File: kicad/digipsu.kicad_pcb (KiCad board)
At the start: 2 copper layers, 137.2 x 174.1 mm, 114 parts, among them J1 Screw_Terminal_01x03, J2 PWR IN, J3 8P8C, J4 8P8C, J5 8P8C, Q1 BC327, Q2 BC337, Q3 2N6058, Q4 2N6058, Q5 IRLZ34N, SW1 RotaryEncoder_Switch, SW2 RotaryEncoder_Switch, U1 INA169, U10 Pico, U11 M24C32-RMN, U12 SN75176BP, U13 6N137, U14 SN75176BP, U15 SN75176BP, U2 MCP6002-xP, U3 Pico, U4 MCP6002-xP, U5 L7805, U6 MCP3464R, U7 LF33_TO220, U8 6N137, U9 SN75176BP

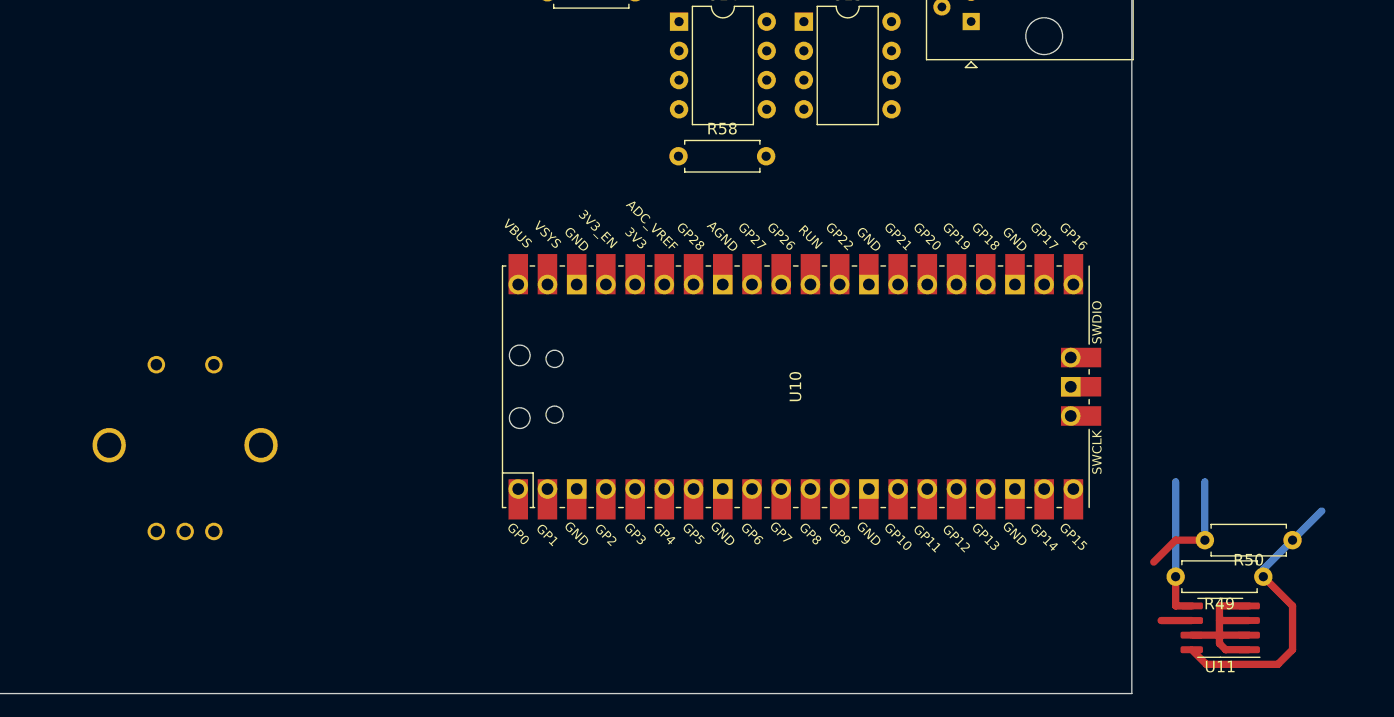
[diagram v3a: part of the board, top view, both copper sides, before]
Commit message: Separate boards automatically
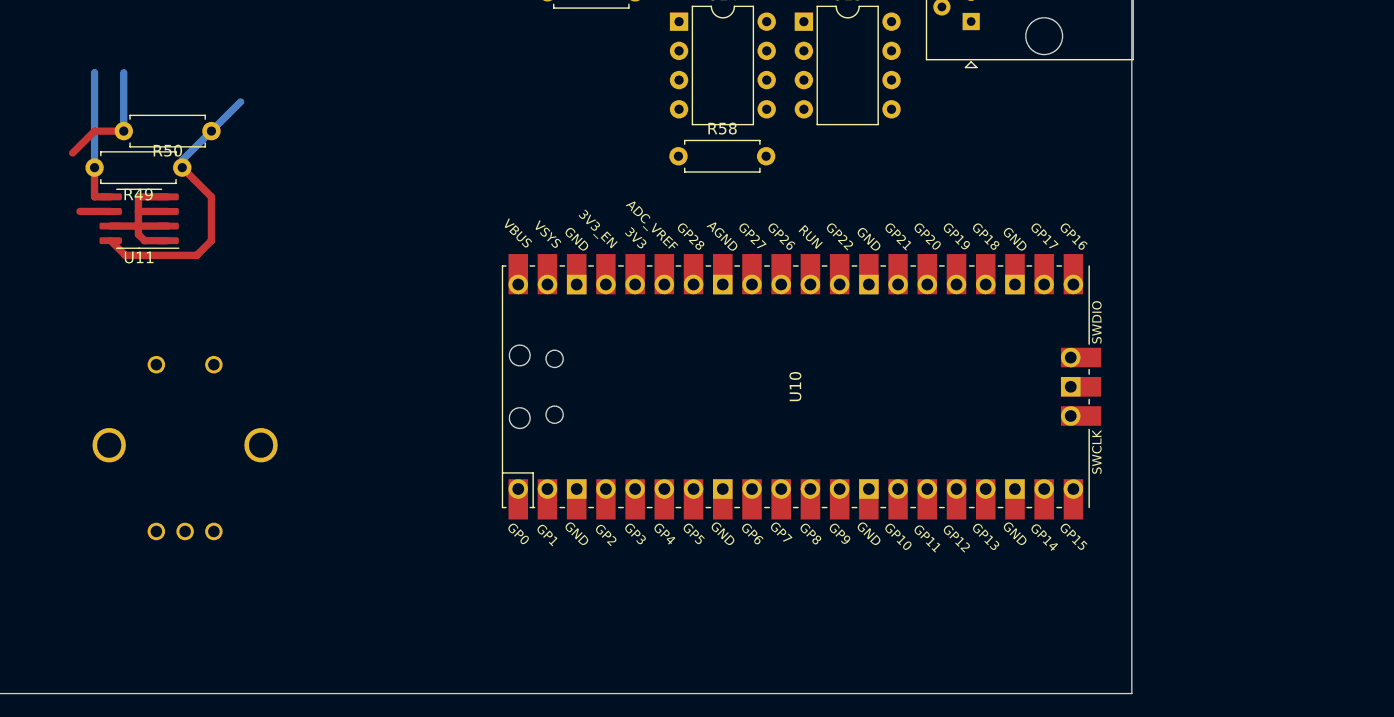
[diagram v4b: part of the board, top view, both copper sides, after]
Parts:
- added B1: Board, PCM_kikit:Board, F.Cu at (27.9, 21.6)
- added B2: Board, PCM_kikit:Board, F.Cu at (27.9, 124.5)
- moved R49 100.5 mm to (68.6, 149.9)
- moved R50 100.5 mm to (71.1, 146.7)
- moved U11 100.5 mm to (64.8, 154.3)
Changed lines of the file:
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@@
     )
   )
+  (footprint "PCM_kikit:Board" (layer "F.Cu")
+    (at 27.94 21.59)
+    (descr "Mark board for extraction")
+    (property "Sheetfile" "controller.kicad_sch")
+    (property "Sheetname" "Controller")
+    (property "exclude_from_bom" "")
+    (property "ki_description" "KiKit Board annotations")
+    (property "ki_keywords" "KiKit")
+    (attr exclude_from_pos_files exclude_from_bom)
+    (fp_text reference "B1" (at -4.5 -5) (layer "Dwgs.User")
+        (effects (font (size 1 1) (thickness 0.15)) (justify left))
+    )
+    (fp_text value "Board" (at -7.25 -5) (layer "Dwgs.User")
+        (effects (font (size 1 1) (thickness 0.15)))
+    )
+    (fp_line (start -1.25 -4) (end -9.25 -4)
+      (stroke (width 0.2) (type solid)) (layer "Dwgs.User"))
+    (fp_line (start 0 0) (end -1.25 -4)
+      (stroke (width 0.2) (type solid)) (layer "Dwgs.User"))
+    (fp_line (start 0 0) (end -1 -0.5)
+      (stroke (width 0.2) (type solid)) (layer "Dwgs.User"))
+    (fp_line (start 0 0) (end 0.5 -1)
+      (stroke (width 0.2) (type solid)) (layer "Dwgs.User"))
+  )
   (footprint "Package_DIP:DIP-8_W7.62mm" (layer "F.Cu")
     (at 32.95 55.81)
@@
   )
   (footprint "Resistor_THT:R_Axial_DIN0207_L6.3mm_D2.5mm_P7.62mm_Horizontal" (layer "F.Cu")
-    (at 165.1 182.245 180)
+    (at 71.12 146.685 180)
     (descr "Resistor, Axial_DIN0207 series, Axial, Horizontal, pin pitch=7.62mm, 0.25W = 1/4W, length*diameter=6.3*2.5mm^2, http://cdn-reichelt.de/documents/datenblatt/B400/1_4W%23YAG.pdf")
     (tags "Resistor Axial_DIN0207 series Axial Horizontal pin pitch 7.62mm 0.25W = 1/4W length 6.3mm diameter 2.5mm")
@@
   )
   (footprint "Package_SO:SOIC-8_3.9x4.9mm_P1.27mm" (layer "F.Cu")
-    (at 158.815 189.865 180)
+    (at 64.835 154.305 180)
     (descr "SOIC, 8 Pin (JEDEC MS-012AA, https://www.analog.com/media/en/package-pcb-resources/package/pkg_pdf/soic_narrow-r/r_8.pdf), generated with kicad-footprint-generator ipc_gullwing_generator.py")
     (tags "SOIC SO")
@@
     )
   )
+  (footprint "PCM_kikit:Board" (layer "F.Cu")
+    (at 27.94 124.46)
+    (descr "Mark board for extraction")
+    (property "Sheetfile" "ui.kicad_sch")
+    (property "Sheetname" "User Interface")
+    (property "exclude_from_bom" "")
+    (property "ki_description" "KiKit Board annotations")
+    (property "ki_keywords" "KiKit")
+    (attr exclude_from_pos_files exclude_from_bom)
+    (fp_text reference "B2" (at -4.5 -5) (layer "Dwgs.User")
+        (effects (font (size 1 1) (thickness 0.15)) (justify left))
+    )
+    (fp_text value "Board" (at -7.25 -5) (layer "Dwgs.User")
+        (effects (font (size 1 1) (thickness 0.15)))
+    )
+    (fp_line (start -1.25 -4) (end -9.25 -4)
+      (stroke (width 0.2) (type solid)) (layer "Dwgs.User"))
+    (fp_line (start 0 0) (end -1.25 -4)
+      (stroke (width 0.2) (type solid)) (layer "Dwgs.User"))
+    (fp_line (start 0 0) (end -1 -0.5)
+      (stroke (width 0.2) (type solid)) (layer "Dwgs.User"))
+    (fp_line (start 0 0) (end 0.5 -1)
+      (stroke (width 0.2) (type solid)) (layer "Dwgs.User"))
+  )
   (footprint "Resistor_THT:R_Axial_DIN0207_L6.3mm_D2.5mm_P7.62mm_Horizontal" (layer "F.Cu")
     (at 107.245 64.7 90)
@@
   )
   (footprint "Resistor_THT:R_Axial_DIN0207_L6.3mm_D2.5mm_P7.62mm_Horizontal" (layer "F.Cu")
-    (at 162.56 185.42 180)
+    (at 68.58 149.86 180)
     (descr "Resistor, Axial_DIN0207 series, Axial, Horizontal, pin pitch=7.62mm, 0.25W = 1/4W, length*diameter=6.3*2.5mm^2, http://cdn-reichelt.de/documents/datenblatt/B400/1_4W%23YAG.pdf")
     (tags "Resistor Axial_DIN0207 series Axial Horizontal pin pitch 7.62mm 0.25W = 1/4W length 6.3mm diameter 2.5mm")
@@
   (dimension (type aligned) (layer "Dwgs.User")
     (pts (xy 17.78 124.475) (xy 151.13 124.475))
-    (height -3.825)
-    (gr_text "133.3500 mm" (at 84.455 119.5) (layer "Dwgs.User")
+    (height -2.555)
+    (gr_text "133.3500 mm" (at 84.455 120.77) (layer "Dwgs.User")
       (effects (font (size 1 1) (thickness 0.15)))
     )
@@
   (segment (start 86.29 25.33) (end 86.29 29.14) (width 0.635) (layer "B.Cu") (net 17))
   (segment (start 78.67 30.41) (end 83.75 30.41) (width 0.635) (layer "B.Cu") (net 17))
-  (segment (start 156.34 187.96) (end 154.94 187.96) (width 0.635) (layer "F.Cu") (net 25))
-  (segment (start 154.94 187.96) (end 154.94 185.42) (width 0.635) (layer "F.Cu") (net 25))
-  (segment (start 154.94 185.42) (end 154.94 177.165) (width 0.635) (layer "B.Cu") (net 25))
-  (segment (start 153.035 184.15) (end 154.94 182.245) (width 0.635) (layer "F.Cu") (net 26))
-  (segment (start 156.34 189.23) (end 153.67 189.23) (width 0.635) (layer "F.Cu") (net 26))
-  (segment (start 154.94 182.245) (end 157.48 182.245) (width 0.635) (layer "F.Cu") (net 26))
-  (segment (start 157.48 182.245) (end 157.48 177.165) (width 0.635) (layer "B.Cu") (net 26))
+  (segment (start 62.36 152.4) (end 60.96 152.4) (width 0.635) (layer "F.Cu") (net 25))
+  (segment (start 60.96 152.4) (end 60.96 149.86) (width 0.635) (layer "F.Cu") (net 25))
+  (segment (start 60.96 149.86) (end 60.96 141.605) (width 0.635) (layer "B.Cu") (net 25))
+  (segment (start 59.055 148.59) (end 60.96 146.685) (width 0.635) (layer "F.Cu") (net 26))
+  (segment (start 62.36 153.67) (end 59.69 153.67) (width 0.635) (layer "F.Cu") (net 26))
+  (segment (start 60.96 146.685) (end 63.5 146.685) (width 0.635) (layer "F.Cu") (net 26))
+  (segment (start 63.5 146.685) (end 63.5 141.605) (width 0.635) (layer "B.Cu") (net 26))
   (segment (start 393.291674 65.586775) (end 393.291674 69.396775) (width 0.635) (layer "B.Cu") (net 57))
   (segment (start 392.021674 64.316775) (end 393.291674 65.586775) (width 0.635) (layer "B.Cu") (net 57))
@@
   (segment (start 65.0225 77.4) (end 68.51 77.4) (width 0.2) (layer "F.Cu") (net 76))
   (segment (start 69.78 76.13) (end 72.955 76.13) (width 0.2) (layer "B.Cu") (net 76))
-  (segment (start 157.61 193.04) (end 163.83 193.04) (width 0.635) (layer "F.Cu") (net 83))
-  (segment (start 165.1 191.77) (end 165.1 187.96) (width 0.635) (layer "F.Cu") (net 83))
-  (segment (start 163.83 193.04) (end 165.1 191.77) (width 0.635) (layer "F.Cu") (net 83))
-  (segment (start 165.1 187.96) (end 162.56 185.42) (width 0.635) (layer "F.Cu") (net 83))
-  (segment (start 156.34 191.77) (end 157.61 193.04) (width 0.635) (layer "F.Cu") (net 83))
-  (segment (start 165.1 182.245) (end 167.64 179.705) (width 0.635) (layer "B.Cu") (net 83))
-  (segment (start 162.56 185.42) (end 162.56 184.785) (width 0.635) (layer "B.Cu") (net 83))
-  (segment (start 162.56 184.785) (end 165.1 182.245) (width 0.635) (layer "B.Cu") (net 83))
+  (segment (start 63.63 157.48) (end 69.85 157.48) (width 0.635) (layer "F.Cu") (net 83))
+  (segment (start 71.12 156.21) (end 71.12 152.4) (width 0.635) (layer "F.Cu") (net 83))
+  (segment (start 69.85 157.48) (end 71.12 156.21) (width 0.635) (layer "F.Cu") (net 83))
+  (segment (start 71.12 152.4) (end 68.58 149.86) (width 0.635) (layer "F.Cu") (net 83))
+  (segment (start 62.36 156.21) (end 63.63 157.48) (width 0.635) (layer "F.Cu") (net 83))
+  (segment (start 71.12 146.685) (end 73.66 144.145) (width 0.635) (layer "B.Cu") (net 83))
+  (segment (start 68.58 149.86) (end 68.58 149.225) (width 0.635) (layer "B.Cu") (net 83))
+  (segment (start 68.58 149.225) (end 71.12 146.685) (width 0.635) (layer "B.Cu") (net 83))
   (segment (start 32.9025 75.584273) (end 32.9025 78.6225) (width 0.635) (layer "B.Cu") (net 84))
   (segment (start 36.8075 74.8125) (end 33.674273 74.8125) (width 0.635) (layer "B.Cu") (net 84))
@@
   (segment (start 113.595 74.86) (end 111.055 77.4) (width 0.635) (layer "B.Cu") (net 107))
   (segment (start 394.561674 69.396775) (end 398.371674 69.396775) (width 0.635) (layer "B.Cu") (net 109))
-  (segment (start 161.29 189.23) (end 158.75 189.23) (width 0.635) (layer "F.Cu") (net 112))
-  (segment (start 158.75 189.23) (end 158.75 190.5) (width 0.635) (layer "F.Cu") (net 112))
-  (segment (start 158.75 191.224132) (end 158.75 190.5) (width 0.635) (layer "F.Cu") (net 112))
-  (segment (start 161.29 187.96) (end 158.75 187.96) (width 0.635) (layer "F.Cu") (net 112))
-  (segment (start 158.75 190.5) (end 161.29 190.5) (width 0.635) (layer "F.Cu") (net 112))
-  (segment (start 161.29 191.77) (end 159.295868 191.77) (width 0.635) (layer "F.Cu") (net 112))
-  (segment (start 159.295868 191.77) (end 158.75 191.224132) (width 0.635) (layer "F.Cu") (net 112))
-  (segment (start 158.75 187.96) (end 158.75 189.23) (width 0.635) (layer "F.Cu") (net 112))
-  (segment (start 156.34 190.5) (end 158.75 190.5) (width 0.635) (layer "F.Cu") (net 112))
+  (segment (start 67.31 153.67) (end 64.77 153.67) (width 0.635) (layer "F.Cu") (net 112))
+  (segment (start 64.77 153.67) (end 64.77 154.94) (width 0.635) (layer "F.Cu") (net 112))
+  (segment (start 64.77 155.664132) (end 64.77 154.94) (width 0.635) (layer "F.Cu") (net 112))
+  (segment (start 67.31 152.4) (end 64.77 152.4) (width 0.635) (layer "F.Cu") (net 112))
+  (segment (start 64.77 154.94) (end 67.31 154.94) (width 0.635) (layer "F.Cu") (net 112))
+  (segment (start 67.31 156.21) (end 65.315868 156.21) (width 0.635) (layer "F.Cu") (net 112))
+  (segment (start 65.315868 156.21) (end 64.77 155.664132) (width 0.635) (layer "F.Cu") (net 112))
+  (segment (start 64.77 152.4) (end 64.77 153.67) (width 0.635) (layer "F.Cu") (net 112))
+  (segment (start 62.36 154.94) (end 64.77 154.94) (width 0.635) (layer "F.Cu") (net 112))
   (segment (start 32.95 60.89) (end 32.315 60.89) (width 0.635) (layer "B.Cu") (net 113))
   (segment (start 32.315 60.89) (end 29.775 63.43) (width 0.635) (layer "B.Cu") (net 113))

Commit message: Add latest changes to fix CI
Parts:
- added C17: 100n, Capacitor_THT:C_Disc_D3.8mm_W2.6mm_P2.50mm, F.Cu at (45.1, 165.7)
- added C301: 100n, Capacitor_THT:C_Disc_D3.8mm_W2.6mm_P2.50mm, F.Cu at (45.1, 168.9)
- added C302: 100n, Capacitor_THT:C_Disc_D3.8mm_W2.6mm_P2.50mm, F.Cu at (45.1, 172.1)
- added C303: 100n, Capacitor_THT:C_Disc_D3.8mm_W2.6mm_P2.50mm, F.Cu at (45.1, 175.3)
- added C304: 100n, Capacitor_THT:C_Disc_D3.8mm_W2.6mm_P2.50mm, F.Cu at (45.1, 178.4)
- added C305: 100n, Capacitor_THT:C_Disc_D3.8mm_W2.6mm_P2.50mm, F.Cu at (45.1, 181.6)
- added C306: 100n, Capacitor_THT:C_Disc_D3.8mm_W2.6mm_P2.50mm, F.Cu at (39.4, 133.3)
- added C307: 100n, Capacitor_THT:C_Disc_D3.8mm_W2.6mm_P2.50mm, F.Cu at (39.4, 136.5)
- added C308: 100n, Capacitor_THT:C_Disc_D3.8mm_W2.6mm_P2.50mm, F.Cu at (39.4, 139.7)
- added C309: 100n, Capacitor_THT:C_Disc_D3.8mm_W2.6mm_P2.50mm, F.Cu at (39.4, 142.9)
- added C310: 100n, Capacitor_THT:C_Disc_D3.8mm_W2.6mm_P2.50mm, F.Cu at (39.4, 146.1)
- added C311: 100n, Capacitor_THT:C_Disc_D3.8mm_W2.6mm_P2.50mm, F.Cu at (39.4, 149.2)
- added R301: 10k, Resistor_THT:R_Axial_DIN0207_L6.3mm_D2.5mm_P7.62mm_Horizontal, F.Cu at (42.5, 165.7)
- added R302: 10k, Resistor_THT:R_Axial_DIN0207_L6.3mm_D2.5mm_P7.62mm_Horizontal, F.Cu at (24.8, 168.9)
- added R303: 10k, Resistor_THT:R_Axial_DIN0207_L6.3mm_D2.5mm_P7.62mm_Horizontal, F.Cu at (42.5, 168.9)
- added R304: 10k, Resistor_THT:R_Axial_DIN0207_L6.3mm_D2.5mm_P7.62mm_Horizontal, F.Cu at (24.8, 172.1)
- added R305: 10k, Resistor_THT:R_Axial_DIN0207_L6.3mm_D2.5mm_P7.62mm_Horizontal, F.Cu at (42.5, 172.1)
- added R306: 10k, Resistor_THT:R_Axial_DIN0207_L6.3mm_D2.5mm_P7.62mm_Horizontal, F.Cu at (24.8, 175.3)
- added R307: 10k, Resistor_THT:R_Axial_DIN0207_L6.3mm_D2.5mm_P7.62mm_Horizontal, F.Cu at (42.5, 175.3)
- added R308: 10k, Resistor_THT:R_Axial_DIN0207_L6.3mm_D2.5mm_P7.62mm_Horizontal, F.Cu at (24.8, 178.4)
- added R309: 10k, Resistor_THT:R_Axial_DIN0207_L6.3mm_D2.5mm_P7.62mm_Horizontal, F.Cu at (42.5, 178.4)
- added R310: 10k, Resistor_THT:R_Axial_DIN0207_L6.3mm_D2.5mm_P7.62mm_Horizontal, F.Cu at (24.8, 181.6)
- added R311: 10k, Resistor_THT:R_Axial_DIN0207_L6.3mm_D2.5mm_P7.62mm_Horizontal, F.Cu at (42.5, 181.6)
- added R312: 10k, Resistor_THT:R_Axial_DIN0207_L6.3mm_D2.5mm_P7.62mm_Horizontal, F.Cu at (19.1, 133.3)
- added R313: 10k, Resistor_THT:R_Axial_DIN0207_L6.3mm_D2.5mm_P7.62mm_Horizontal, F.Cu at (36.8, 133.3)
- added R314: 10k, Resistor_THT:R_Axial_DIN0207_L6.3mm_D2.5mm_P7.62mm_Horizontal, F.Cu at (19.1, 136.5)
- added R315: 10k, Resistor_THT:R_Axial_DIN0207_L6.3mm_D2.5mm_P7.62mm_Horizontal, F.Cu at (36.8, 136.5)
- added R316: 10k, Resistor_THT:R_Axial_DIN0207_L6.3mm_D2.5mm_P7.62mm_Horizontal, F.Cu at (19.1, 139.7)
- added R317: 10k, Resistor_THT:R_Axial_DIN0207_L6.3mm_D2.5mm_P7.62mm_Horizontal, F.Cu at (36.8, 139.7)
- added R318: 10k, Resistor_THT:R_Axial_DIN0207_L6.3mm_D2.5mm_P7.62mm_Horizontal, F.Cu at (19.1, 142.9)
- added R319: 10k, Resistor_THT:R_Axial_DIN0207_L6.3mm_D2.5mm_P7.62mm_Horizontal, F.Cu at (36.8, 142.9)
- added R320: 10k, Resistor_THT:R_Axial_DIN0207_L6.3mm_D2.5mm_P7.62mm_Horizontal, F.Cu at (19.1, 146.1)
- added R321: 10k, Resistor_THT:R_Axial_DIN0207_L6.3mm_D2.5mm_P7.62mm_Horizontal, F.Cu at (36.8, 146.1)
- added R322: 10k, Resistor_THT:R_Axial_DIN0207_L6.3mm_D2.5mm_P7.62mm_Horizontal, F.Cu at (19.1, 149.2)
- added R323: 10k, Resistor_THT:R_Axial_DIN0207_L6.3mm_D2.5mm_P7.62mm_Horizontal, F.Cu at (36.8, 149.2)
- added R61: 10k, Resistor_THT:R_Axial_DIN0207_L6.3mm_D2.5mm_P7.62mm_Horizontal, F.Cu at (24.8, 165.7)
- added U16: 74AC14, Package_SO:SOIC-14_3.9x8.7mm_P1.27mm, F.Cu at (55.2, 174.0)
- added U301: 74AC14, Package_SO:SOIC-14_3.9x8.7mm_P1.27mm, F.Cu at (48.9, 141.0)
- moved J1 174.5 mm to (175.3, 66.3)
- moved NT3 174.5 mm to (220.0, 70.2)
- moved Q2 174.5 mm to (220.0, 91.2)
- moved R2 174.5 mm to (189.3, 110.7)
- moved R3 174.5 mm to (189.3, 114.8)
- moved R34 174.5 mm to (219.1, 93.1)
- moved R4 174.5 mm to (147.6, 87.6)
- moved R5 174.5 mm to (216.2, 98.8)
- moved R8 174.5 mm to (147.6, 101.7)
- moved F1 174.5 mm to (200.6, 112.7)
- moved J2 174.5 mm to (146.1, 69.6)
- moved NT2 174.5 mm to (204.8, 70.2)
- moved Q4 174.5 mm to (245.0, 96.9)
- moved R1 174.5 mm to (204.8, 72.8)
- moved R37 174.5 mm to (168.0, 54.8)
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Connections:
- SW1 pad A: unconnected-(SW1-PadA) -> /User Interface/SWin5
- SW1 pad B: unconnected-(SW1-PadB) -> /User Interface/SWin6
- SW1 pad C: unconnected-(SW1-PadC) -> /User Interface/GND
- SW1 pad S1: unconnected-(SW1-PadS1) -> /User Interface/SWin4
- SW1 pad S2: unconnected-(SW1-PadS2) -> /User Interface/GND
- SW2 pad A: unconnected-(SW2-PadA) -> /User Interface/SWin2
- SW2 pad B: unconnected-(SW2-PadB) -> /User Interface/SWin3
- SW2 pad C: unconnected-(SW2-PadC) -> /User Interface/GND
- SW2 pad S1: unconnected-(SW2-PadS1) -> /User Interface/SWin1
- SW2 pad S2: unconnected-(SW2-PadS2) -> /User Interface/GND
- U10 pad 1: unconnected-(U10-GPIO0-Pad1) -> /User Interface/SWout1
- U10 pad 2: unconnected-(U10-GPIO1-Pad2) -> /User Interface/SWout2
- U10 pad 4: unconnected-(U10-GPIO2-Pad4) -> /User Interface/SWout3
- U10 pad 5: unconnected-(U10-GPIO3-Pad5) -> /User Interface/SWout4
- U10 pad 6: unconnected-(U10-GPIO4-Pad6) -> /User Interface/SWout5
- U10 pad 7: unconnected-(U10-GPIO5-Pad7) -> /User Interface/SWout6
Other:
- board size 137.2 x 174.1 mm -> 137.2 x 174 mm

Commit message: Compile gerber and drill files in one zip
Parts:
- moved SW1 62.5 mm to (57.1, 192.0)
- moved SW2 62.3 mm to (33.4, 191.7)
- moved C307 27.1 mm to (66.0, 131.4)
- moved C309 27.1 mm to (66.0, 137.8)
- moved C310 27.1 mm to (66.0, 141.0)
- moved C306 27.1 mm to (66.0, 128.3)
- moved C308 27.1 mm to (66.0, 134.6)
- moved C311 27.1 mm to (66.0, 144.1)
- moved R315 27.1 mm to (63.5, 131.4)
- moved R319 27.1 mm to (63.5, 137.8)
- moved R321 27.1 mm to (63.5, 141.0)
- moved R314 27.1 mm to (45.7, 131.4)
- moved R318 27.1 mm to (45.7, 137.8)
- moved R320 27.1 mm to (45.7, 141.0)
- moved R313 27.1 mm to (63.5, 128.3)
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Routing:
- net /User Interface/GND: track 0.00 -> 24.2 mm
- net Net-(C17-Pad1): track 0.00 -> 21.9 mm
- net Net-(C305-Pad1): track 0.00 -> 20.0 mm
- net Net-(C301-Pad1): track 0.00 -> 17.3 mm
- net Net-(C304-Pad1): track 0.00 -> 16.5 mm
- net +3.3V: track 25.0 -> 40.9 mm
- net Net-(C302-Pad1): track 0.00 -> 13.1 mm
- net Net-(C303-Pad1): track 0.00 -> 11.5 mm
- net /User Interface/SWin6: track 0.00 -> 2.54 mm
- net /User Interface/SWin5: track 0.00 -> 2.54 mm
- net /User Interface/SWin4: track 0.00 -> 2.54 mm
- net /User Interface/SWin3: track 0.00 -> 2.54 mm
- net /User Interface/SWin2: track 0.00 -> 2.54 mm
- net /User Interface/SWin1: track 0.00 -> 2.54 mm
- net /User Interface/SWout6: track 0.00 -> 1.97 mm, vias 0 -> 1
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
